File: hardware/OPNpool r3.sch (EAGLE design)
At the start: 16 parts, among them J2 RS485-TERM-SPTAF, J3 ESP-JTAG-2X05, SW1 Factory (5 sec), U1 MAX3485CSA+

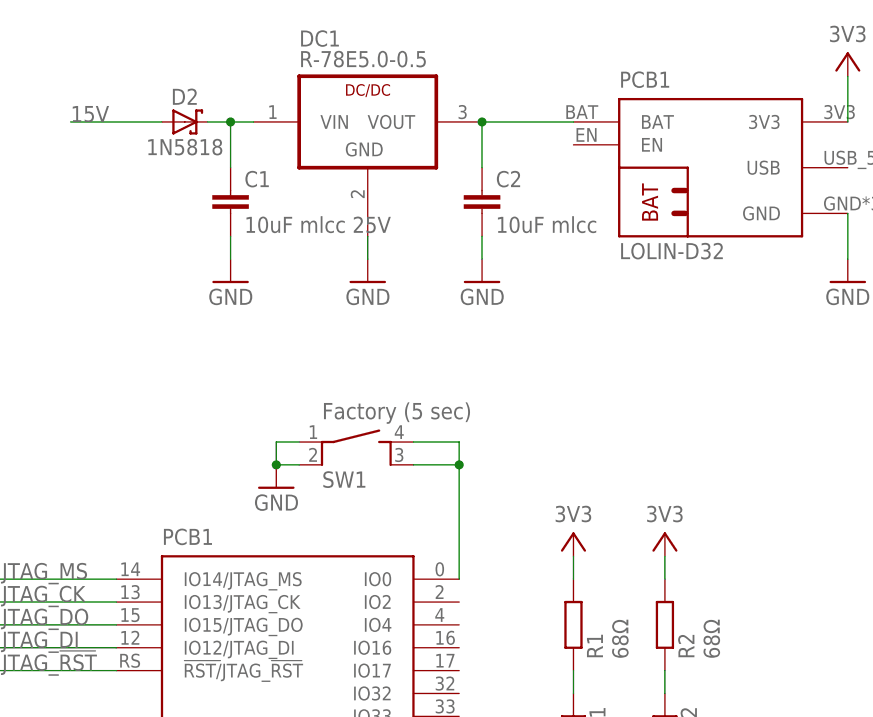
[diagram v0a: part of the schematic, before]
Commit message: routed pcb r3
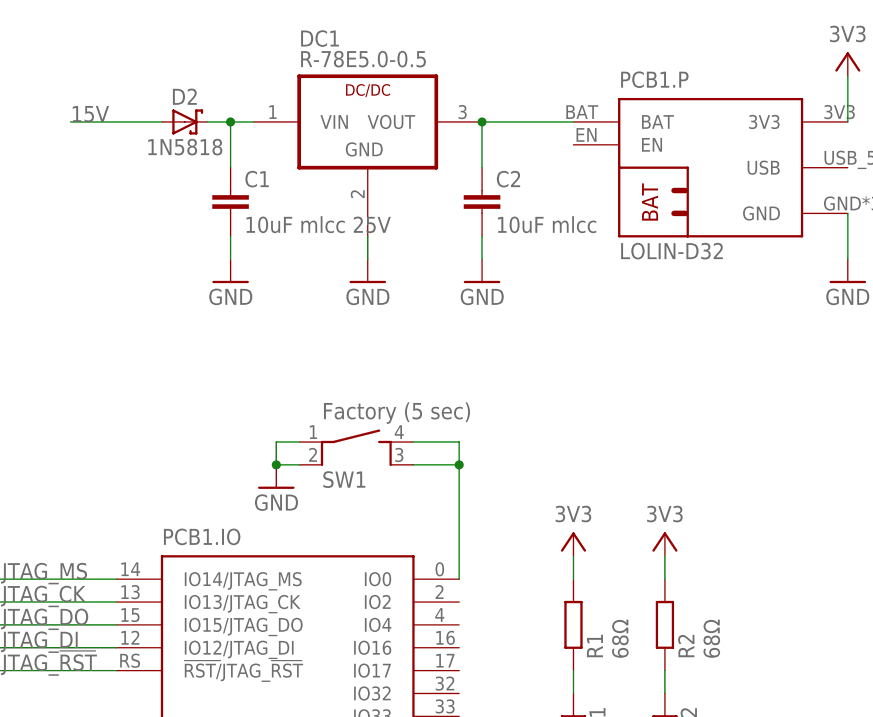
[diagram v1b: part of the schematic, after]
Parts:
- PCB1: device Coert Vonk:LOLIN-D32 -> Coert-Vonk:LOLIN-D32; ALIEXPRESS# 32808551116 -> (none); MANF WEMOS Electronics -> (none); MANF# D32 -> (none)
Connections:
- net 3V3: now also PCB1.P.3V3; no longer PCB1P.3V3
- net GND: now also PCB1.IO.I34, PCB1.IO.VN/I39, PCB1.IO.VP/I36, PCB1.P.GND; no longer PCB1G$1.I34, PCB1G$1.VN/I39, PCB1G$1.VP/I36, PCB1P.GND
- net JTAG_!RST: now also PCB1.IO.!RST/!JTAG_!RST; no longer PCB1G$1.!RST/!JTAG_!RST
- net JTAG_CK: now also PCB1.IO.IO13/JTAG_CK; no longer PCB1G$1.IO13/JTAG_CK
- net JTAG_DI: now also PCB1.IO.IO12/JTAG_DI; no longer PCB1G$1.IO12/JTAG_DI
- net JTAG_DO: now also PCB1.IO.IO15/JTAG_DO; no longer PCB1G$1.IO15/JTAG_DO
- net JTAG_MS: now also PCB1.IO.IO14/JTAG_MS; no longer PCB1G$1.IO14/JTAG_MS
- net N$3: now also PCB1.IO.IO0; no longer PCB1G$1.IO0
- net RTS: now also PCB1.IO.RTS2/IO27; no longer PCB1G$1.RTS2/IO27
- net RX2: now also PCB1.IO.RX2/IO25; no longer PCB1G$1.RX2/IO25
- net TX: now also PCB1.IO.TX2/IO26; no longer PCB1G$1.TX2/IO26
- net VOUT: now also PCB1.P.BAT; no longer PCB1P.BAT
